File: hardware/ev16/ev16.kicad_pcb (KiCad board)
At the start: 4 copper layers, 125 x 80 mm, 168 parts, among them CN1 Conn_05x02_Female, CN2 PJ-242, J1 USB_C_Receptacle, J10 Conn_01x03_Pin, J11 Conn_02x05_Counter_Clockwise, J2 Conn_01x02_Socket, J3 AudioJack4, J4 Conn_02x03_Odd_Even, J5 Conn_02x03_Odd_Even, J6 Conn_02x05_Counter_Clockwise, J7 Conn_02x05_Counter_Clockwise, J8 Conn_02x05_Counter_Clockwise, J9 Conn_02x05_Counter_Clockwise, Q1 2N7002, Q2 2N7002, SW1 SW_SPDT, SW2 SW_Push, SW3 SW_Push, SW4 SW_Push, SW5 SW_Push, SW6 SW_Push, SW7 SW_Push, U1 BQ21040DBV, U10 STM32F405RGTx, U2 USBLC6-2P6, U3 STM32F072CBTx, U4 CH340C, U5 TPS63060, U6 WM8960CGEFL/RV, U7 ESP32-S3-WROOM-1, U8 M24C02-RMN6TP, Y1 Crystal_GND24

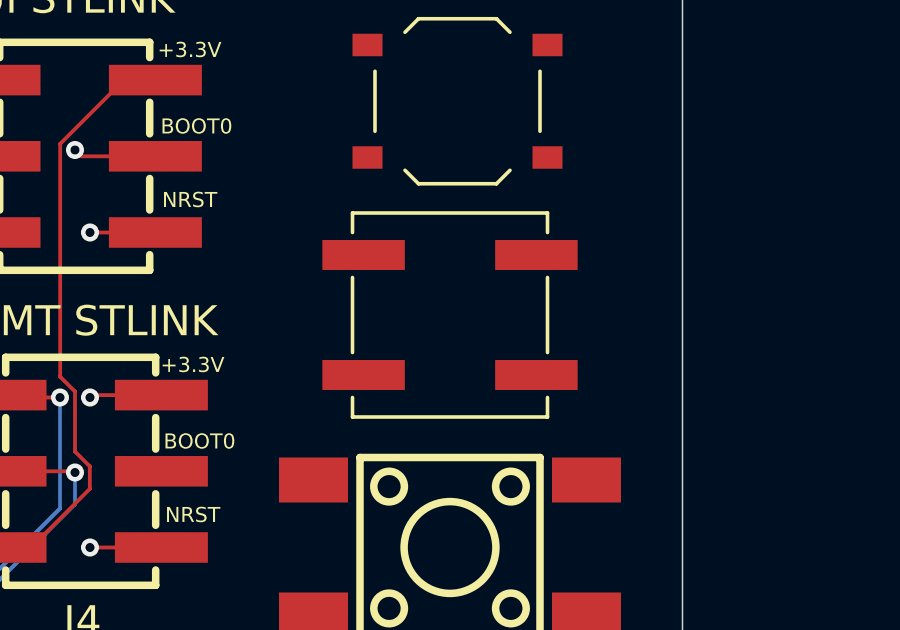
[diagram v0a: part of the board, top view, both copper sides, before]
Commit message: fixed wrong jlcpcb part numbers
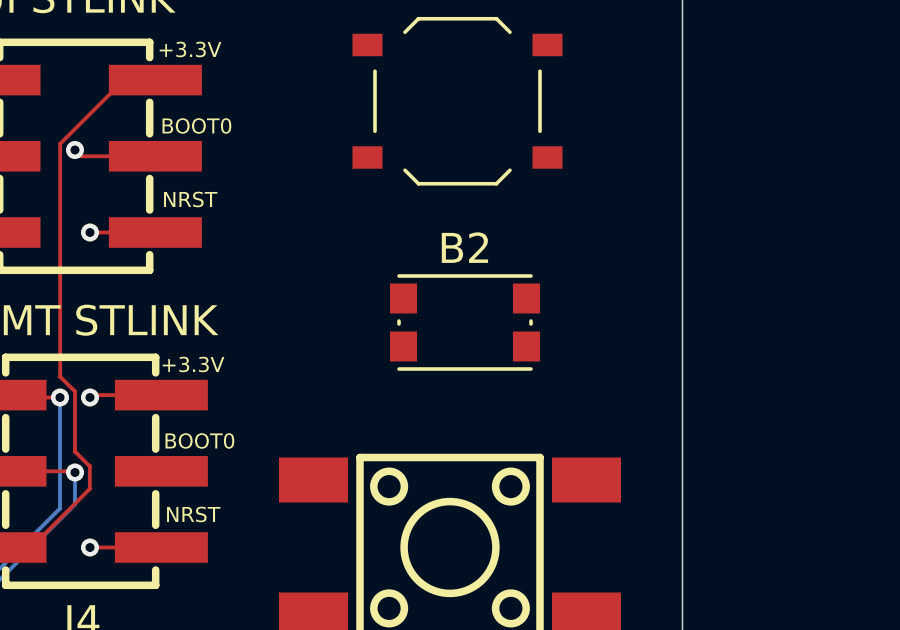
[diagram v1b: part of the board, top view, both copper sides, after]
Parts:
- removed REF**: SW_SPST_B3SL-1022P, Button_Switch_SMD:SW_SPST_B3SL-1022P
- added B2: SW_Push_1P1T_NO_CK_KMR2, Button_Switch_SMD:SW_Push_1P1T_NO_CK_KMR2, F.Cu at (167.8, 89.5)
- renumbered REF** to B1, REF** to B3, REF** to B4

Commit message: Update R12 to 10k for battery monitor
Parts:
- R12: value 4k7 -> 10k
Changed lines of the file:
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@@
 			)
 		)
-		(property "Value" "4k7"
+		(property "Value" "10k"
 			(at 0 1.17 90)
 			(layer "F.Fab")
@@
 			)
 		)
-		(property "JLCPCB Part #" "C25900"
+		(property "JLCPCB Part #" "C25744"
 			(at 0 0 270)
 			(unlocked yes)

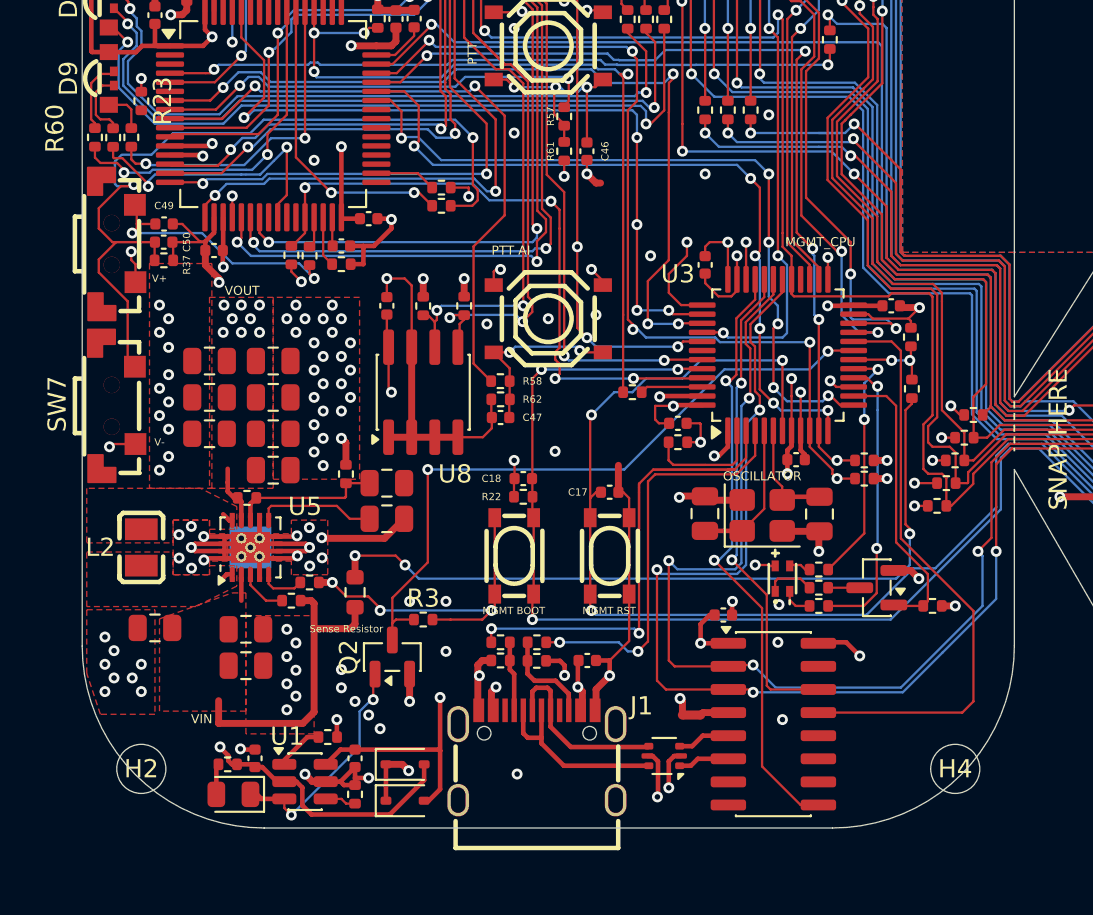
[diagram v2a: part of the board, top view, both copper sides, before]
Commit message: feat: added auto reset mosfet to mgmt chip from usb
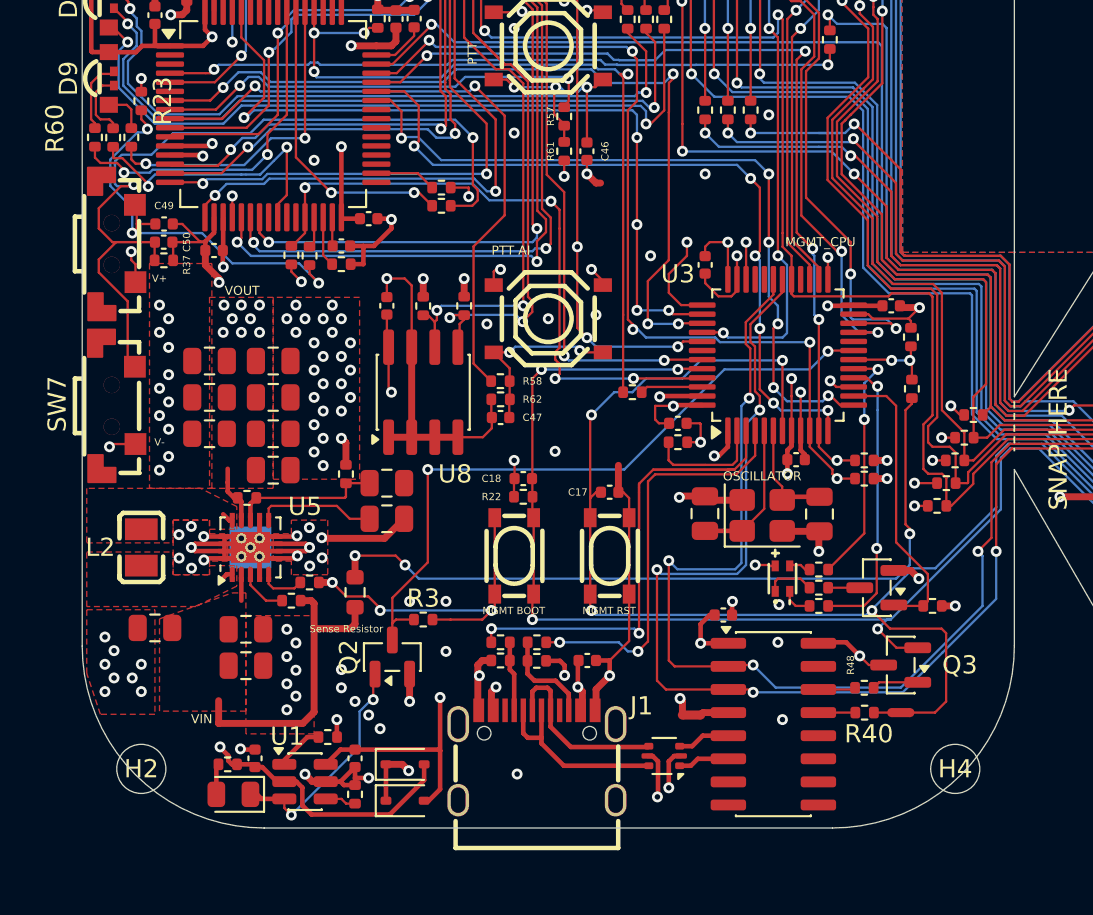
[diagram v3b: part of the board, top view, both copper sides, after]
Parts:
- added NT3: NetTie_2, NetTie:NetTie-2_SMD_Pad0.5mm, F.Cu at (95.0, 103.7)
- added Q3: 2N7002, Package_TO_SOT_SMD:SOT-23, F.Cu at (95.0, 101.0)
- added R40: 1k0, Resistor_SMD:R_0402_1005Metric, F.Cu at (93.0, 103.7)
- added R48: 1k0, Resistor_SMD:R_0402_1005Metric, F.Cu at (93.0, 102.3)
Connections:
- U3 pad 20: /USB_DTR_MGMT -> unconnected-(U3-PB2-Pad20)
- U3 pad 32: /USB_RTS_MGMT -> unconnected-(U3-PA11-Pad32)
- U3 pad 33: /USB_CTS_MGMT -> unconnected-(U3-PA12-Pad33)
- U4 pad 13: /USB_DTR_MGMT -> Net-(U4-~{DTR})
- U4 pad 14: /USB_RTS_MGMT -> Net-(U4-~{RTS})
- U4 pad 9: /USB_CTS_MGMT -> unconnected-(U4-~{CTS}-Pad9)
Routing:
- net /USB_CTS_MGMT: track 33.4 -> 0.00 mm, vias 2 -> 0
- net /USB_DTR_MGMT: track 32.5 -> 0.00 mm
- net /USB_RTS_MGMT: track 26.8 -> 0.00 mm, vias 2 -> 0
- net /MGMT_NRST: track 121.6 -> 132.5 mm, vias 4 -> 5
- net Net-(C49-Pad1): track 14.6 -> 23.8 mm, vias 2 -> 3
- net /MGMT_BOOT: track 119.0 -> 122.6 mm, vias 4 -> 5
- net /USB_RTS: track 0.00 -> 2.55 mm
- net Net-(U4-~{RTS}): track 0.00 -> 2.19 mm
- net Net-(U4-~{DTR}): track 0.00 -> 2.03 mm
- net +3.3V: track 306.0 -> 307.5 mm
- net /USB_DTR: track 0.00 -> 0.98 mm

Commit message: production generator push
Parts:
- removed C18: 100n, Capacitor_SMD:C_0402_1005Metric
- removed R48: 1k0, Resistor_SMD:R_0402_1005Metric
- added R51: 4k7, Resistor_SMD:R_0402_1005Metric, F.Cu at (93.0, 102.5)
- added R75: 100k, Resistor_SMD:R_0402_1005Metric, F.Cu at (95.2, 102.8)
- moved R22 5.94 mm to (76.5, 86.3)
- moved Q3 1.12 mm to (96.0, 100.5)
- moved NT3 0.13 mm to (95.0, 103.8)
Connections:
- NT3 pad 1: /USB_DTR -> Net-(NT3-Pad1)
- Q3 pad 1: /USB_RTS -> Net-(Q3-G)
- Q3 pad 2: /MGMT_BOOT -> GND
- Q3 pad 3: +3.3V -> /MGMT_BOOT
- R22 pad 1: GND -> /MGMT_BOOT
- R22 pad 2: /MGMT_BOOT -> +3.3V
- R40 pad 1: /USB_DTR -> Net-(NT3-Pad1)
- R40 pad 2: Net-(U4-~{DTR}) -> /USB_DTR
- SW2 pad 1: +3.3V -> GND
- SW2 pad 2: +3.3V -> GND
- SW2 pad 3: /MGMT_BOOT -> Net-(Q3-G)
- SW2 pad 4: /MGMT_BOOT -> Net-(Q3-G)
- U4 pad 13: Net-(U4-~{DTR}) -> /USB_DTR
- U4 pad 14: Net-(U4-~{RTS}) -> /USB_RTS
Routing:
- net Net-(Q3-G): track 0.00 -> 31.3 mm, vias 0 -> 2
- net +3.3V: track 307.5 -> 296.4 mm, vias 45 -> 47
- net GND: track 309.9 -> 312.3 mm, vias 147 -> 144
- net /USB_RX1_MGMT: track 97.4 -> 99.9 mm
- net /USB_TX1_MGMT: track 90.9 -> 93.3 mm
- net Net-(U4-~{RTS}): track 2.19 -> 0.00 mm
- net Net-(U4-~{DTR}): track 2.03 -> 0.00 mm
- net /MGMT_NRST: track 132.5 -> 130.8 mm
- net /USB_DTR: track 0.98 -> 2.03 mm
- net Net-(NT3-Pad1): track 0.00 -> 1.04 mm
- net /MGMT_BOOT: track 122.6 -> 121.8 mm
- net /USB_CC2_DETECT: track 32.5 -> 33.2 mm
- net /USB_CC1_DETECT: track 22.7 -> 23.4 mm
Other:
- board text added: "EV16MK1"
- board text removed: "EV16"
